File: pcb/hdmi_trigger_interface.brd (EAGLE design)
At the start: 78.7 x 63.5 mm, 58 parts, among them U1 TPD12S016PWR, U2 TPD12S016PWR, Y1 SI514

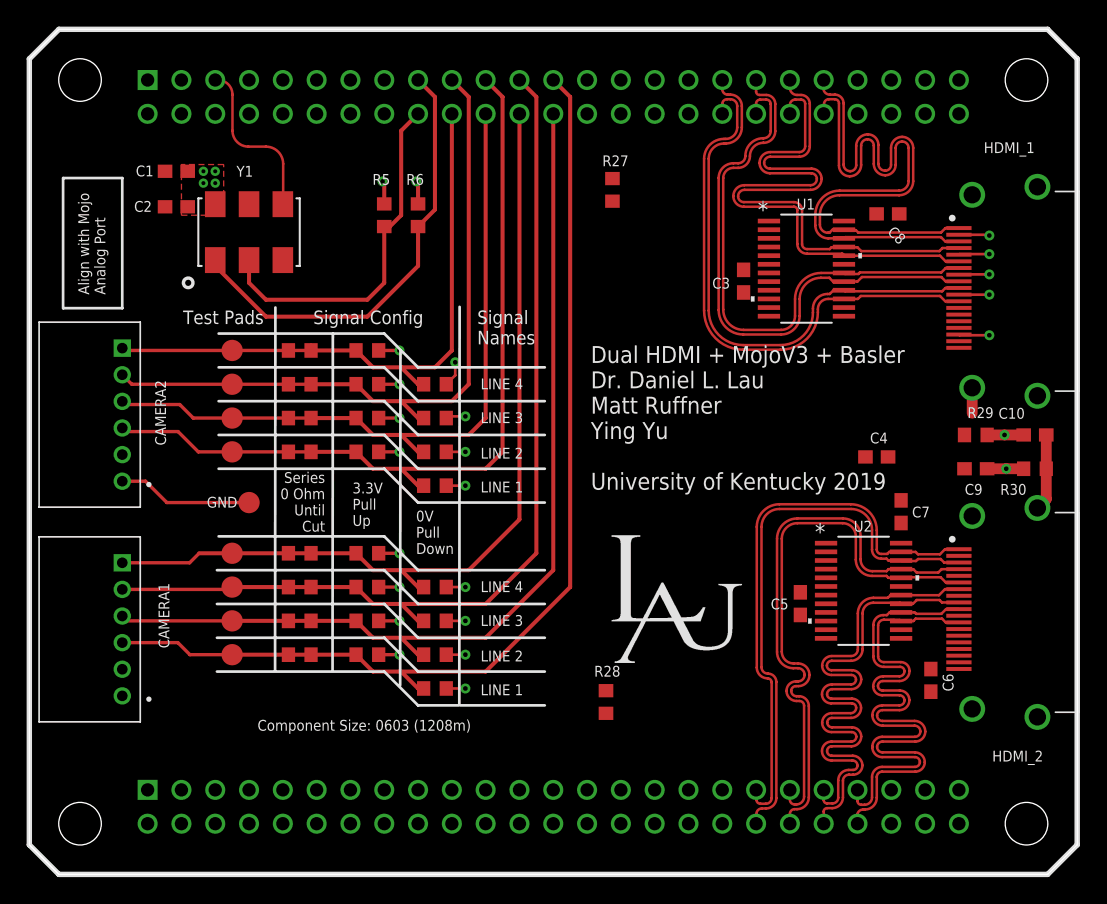
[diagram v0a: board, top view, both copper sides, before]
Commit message: length tuning and routing done, need final review then ready to order
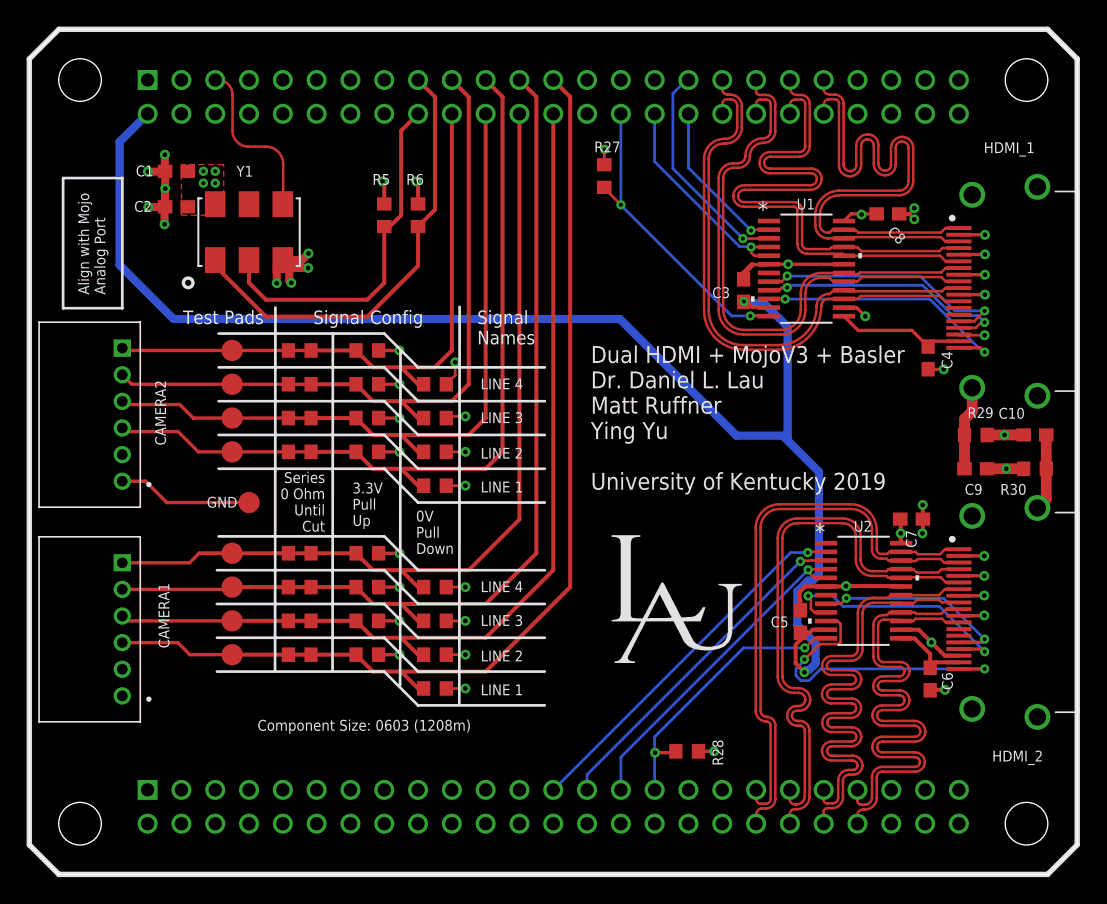
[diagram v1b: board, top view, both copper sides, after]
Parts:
- moved C4 8.38 mm to (67.5, 38.8), turned to 270 degrees
- moved R28 7.14 mm to (49.4, 9.25), turned to 180 degrees
- moved C5 1.35 mm to (57.9, 19.0)
- moved R27 1.21 mm to (43.2, 52.5)
- moved C7 0.97 mm to (66.3, 26.7), turned to 0 degrees
- moved C3 0.71 mm to (53.7, 43.9)
- moved C6 0.11 mm to (67.7, 14.7)
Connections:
- net HP1_M: now also U$1.5
- net HP2_M: now also U$1.100
- net SCL2_M: now also U$1.95; no longer U$1.112
- net SDA2_M: now also U$1.98; no longer U$1.111
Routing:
- net 5V: track 0.00 -> 108.3 mm, vias 0 -> 2
- net GND: track 39.2 -> 92.9 mm, vias 15 -> 38
- net SCL2_M: track 0.00 -> 27.9 mm, vias 0 -> 1
- net SDA2_M: track 0.00 -> 25.8 mm, vias 0 -> 1
- net HP2_M: track 0.00 -> 25.4 mm, vias 0 -> 1
- net HP2: track 0.00 -> 23.9 mm, vias 0 -> 2
- net CTHPD1: track 0.00 -> 23.9 mm, vias 0 -> 2
- net CTHPD2: track 0.00 -> 21.6 mm, vias 0 -> 2
- net HP1: track 0.00 -> 19.9 mm, vias 0 -> 2
- net SCL1: track 0.00 -> 19.7 mm, vias 0 -> 2
- net SDA1: track 0.00 -> 19.6 mm, vias 0 -> 2
- net SDA2: track 0.00 -> 19.3 mm, vias 0 -> 2
- net SDA1_M: track 0.00 -> 16.7 mm, vias 0 -> 1
- net HP1_M: track 0.00 -> 16.7 mm, vias 0 -> 1
- net SCL2: track 0.00 -> 15.4 mm, vias 0 -> 2
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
